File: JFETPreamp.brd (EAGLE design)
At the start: 52.7 x 27.6 mm, 30 parts, among them IC1 ICL7660CBA, IC2 LF356MX, IC3 LF356MX, J1 Input, J2 5V In, J3 Range Select, J4 Output

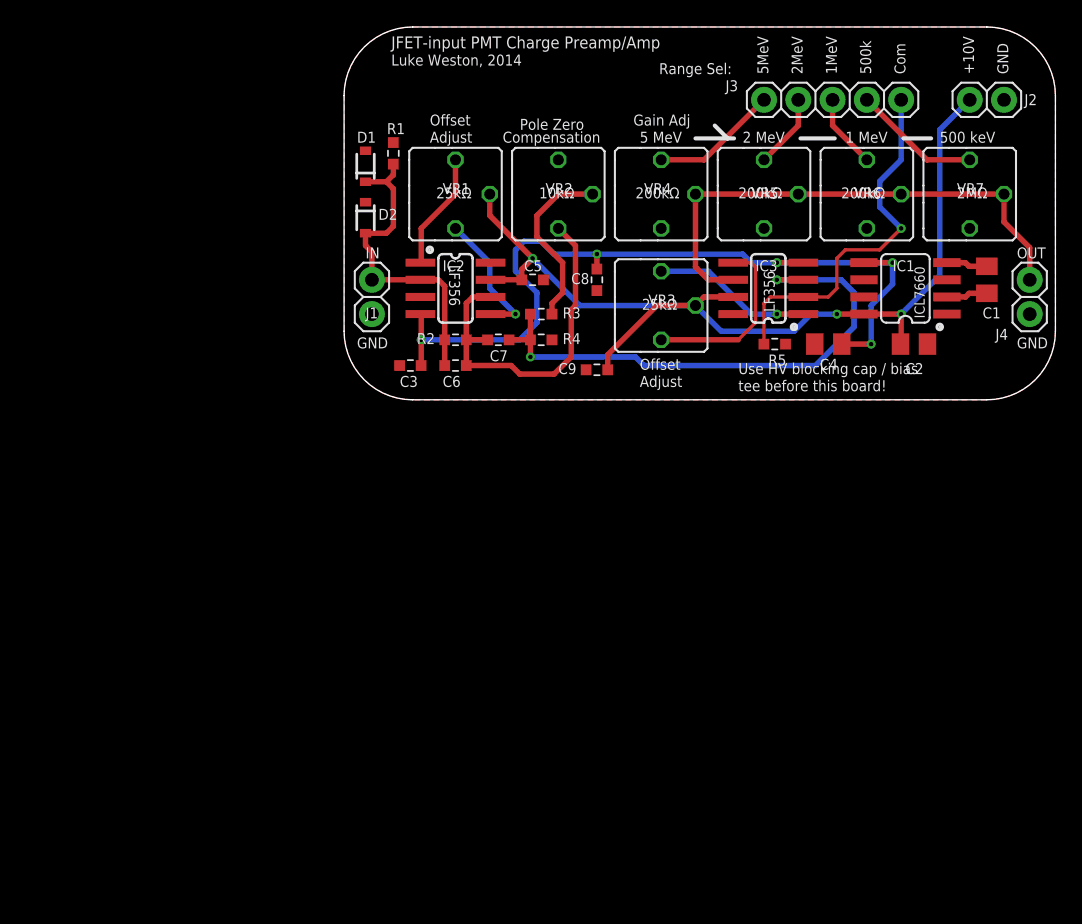
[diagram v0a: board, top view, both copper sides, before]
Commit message: changed to single dual opamp
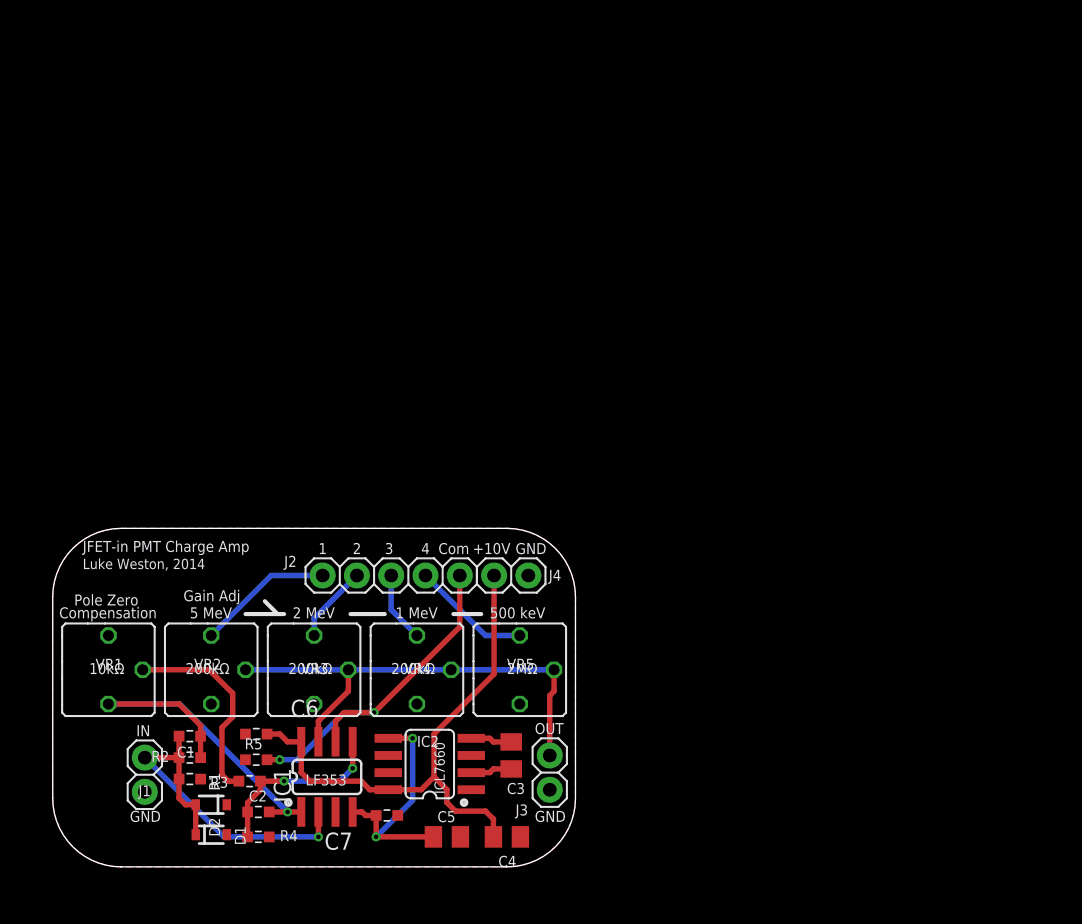
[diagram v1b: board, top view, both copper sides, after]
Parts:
- removed C8, C9: 68nF, freetronics-luke:0603
- removed IC3: LF356MX, linear:SO08
- removed VR6: 200kΩ, pot:B25P
- removed VR7: 2MΩ, pot:B25P
- C1, C2: value 10µF -> 110pF; device rcl:C0805K -> freetronics-luke:0603
- C3, C5: value 68nF -> 10µF; device freetronics-luke:0603 -> rcl:C0805K
- C6, C7: value 110pF -> 68nF
- IC1: value ICL7660CBA -> LF353D; device maxim:SO08 -> linear:SO08
- IC2: value LF356MX -> ICL7660CBA; device linear:SO08 -> maxim:SO08
- J2: value 5V In -> Range Select; device pinhead:1X02 -> pinhead:1X05
- J3: value Range Select -> Output; device pinhead:1X05 -> pinhead:1X02
- J4: value Output -> 5V In
- VR1: value 25kΩ -> 10kΩ
- VR2: value 10kΩ -> 200kΩ
- VR3: value 25kΩ -> 200kΩ
- VR5: value 200kΩ -> 2MΩ
- moved C1 68.1 mm to (12.1, 11.9), turned to 0 degrees
- moved C2 59.7 mm to (17.1, 6.29), turned to 180 degrees
- moved J2 56.5 mm to (27.0, 23.8), turned to 180 degrees
- moved IC1 56.1 mm to (22.2, 8.89), turned to 0 degrees
- moved J3 54.1 mm to (38.7, 9.21), turned to 270 degrees
- moved D1 50.8 mm to (13.7, 4.60), turned to 0 degrees
- moved R5 49.2 mm to (17.0, 10.2), turned to 180 degrees
- moved R1 48.8 mm to (12.1, 8.73), turned to 180 degrees
- moved D2 45.0 mm to (13.7, 6.83), turned to 180 degrees
- moved VR1 43.6 mm to (6.03, 16.8)
- moved VR2 43.6 mm to (13.7, 16.8)
- moved J4 43.6 mm to (35.9, 23.8), turned to 0 degrees
- moved C4 43.6 mm to (35.6, 4.45), turned to 0 degrees
- moved R4 42.4 mm to (17.1, 4.45)
- moved C5 41.8 mm to (31.1, 4.45), turned to 0 degrees
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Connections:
- removed net +5V: C2.1, C5.2, C9.2, IC1.8, IC2.7, IC3.7, J2.1, VR1.S, VR3.S
- removed net -5V: C3.2, C4.1, C8.2, IC1.5, IC2.4, IC3.4
- removed net N$12: IC3.5, VR3.E
- removed net N$14: IC2.5, VR1.E
- net GND: now also C5.2, C6.1, C7.1, J3.2, VR1.A; no longer C2.2, C3.1, C5.1, C8.1, C9.1, J2.2, VR2.A
- net N$1: now also C1.1, IC1.2; no longer C6.1, IC2.2
- net N$10: now also J2.2, VR5.A; no longer J3.2, VR7.A
- net N$11: now also C5.1, C7.2, IC1.4, IC2.5; no longer IC3.1, VR3.A
- net N$13: now also C4.1, C6.2, IC1.8, IC2.8, J4.1; no longer IC2.1, VR1.A
- net N$15: now also C3.1, IC2.2; no longer C1.1, IC1.2
- net N$16: now also C3.2, IC2.4; no longer C1.2, IC1.4
- net N$2: now also C2.2, IC1.5; no longer C7.2, IC3.3
- net N$3: now also C1.2, C2.1, IC1.1, VR1.E; no longer C6.2, C7.1, IC2.6, VR2.E
- net N$4: now also IC1.6, J2.1; no longer IC3.2, J3.1
- net N$5: now also VR1.S; no longer VR2.S
- net N$6: now also J2.5, VR2.A; no longer J3.5, VR4.A
- net N$7: now also IC1.7, J3.1, VR2.S, VR3.S; no longer IC3.6, J4.1, VR6.S, VR7.S
- net N$8: now also J2.4, VR3.A; no longer J3.4, VR5.A
- net N$9: now also J2.3, VR4.A; no longer J3.3, VR6.A
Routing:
- net +5V: track 73.3 -> 0.00 mm, vias 3 -> 0
- net -5V: track 61.9 -> 0.00 mm, vias 5 -> 0
- net N$13: track 8.70 -> 40.1 mm
- net N$2: track 40.8 -> 13.7 mm
- net N$12: track 13.4 -> 0.00 mm
- net N$14: track 10.0 -> 0.00 mm, vias 1 -> 0
- net N$11: track 11.9 -> 17.9 mm, vias 1 -> 2
- net N$1: track 24.0 -> 27.9 mm, vias 0 -> 1
- net N$7: track 39.2 -> 35.6 mm
- net N$5: track 13.2 -> 15.2 mm
- net N$3: track 26.9 -> 28.8 mm, vias 0 -> 1
- net N$4: track 27.6 -> 26.8 mm, vias 1 -> 2
- net N$6: track 9.46 -> 10.1 mm
- net N$10: track 9.46 -> 8.83 mm
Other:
- board size 52.7 x 27.6 mm -> 38.7 x 25.1 mm
- board text added: "1"
- board text added: "2"
- board text added: "3"
- board text added: "4"
- board text added: "JFET-in PMT Charge Amp"
- board text added: "LF353"
- board text removed: "1MeV"
- board text removed: "25kΩ"
- board text removed: "2MeV"
- board text removed: "500k"
- board text removed: "5MeV"
- board text removed: "Adjust"
- board text removed: "JFET-input PMT Charge Preamp/Amp"
- board text removed: "LF356"
- board text removed: "Offset"
- board text removed: "Range Sel:"
- board text removed: "Use HV blocking cap / bias"
- board text removed: "tee before this board!"

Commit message: foo
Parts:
- moved C4 0.95 mm to (34.6, 4.45)
- moved C5 0.95 mm to (30.2, 4.45)
- moved J3 0.32 mm to (39.1, 9.21)
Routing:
- net N$4: track 26.8 -> 31.0 mm
- net N$1: track 27.9 -> 24.4 mm, vias 1 -> 0
- net N$11: track 17.9 -> 17.0 mm
- net N$13: track 40.1 -> 39.3 mm

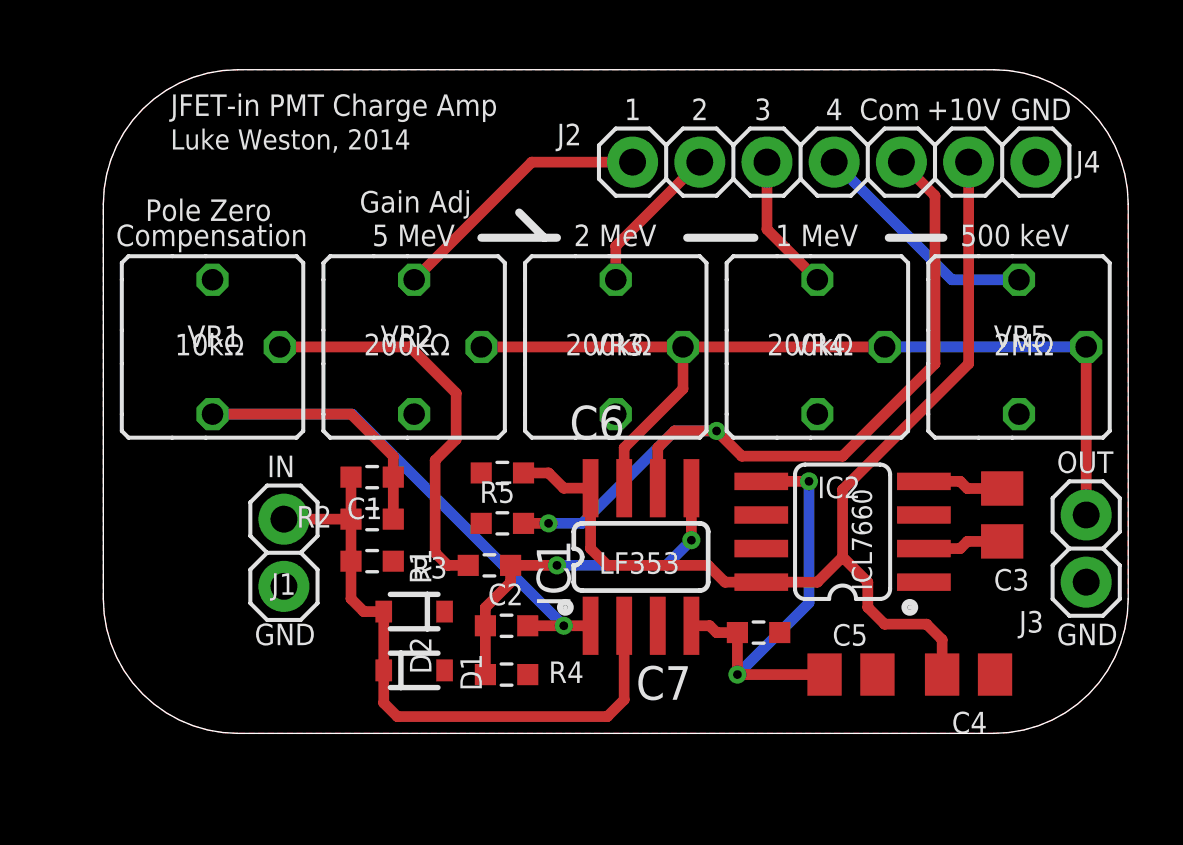
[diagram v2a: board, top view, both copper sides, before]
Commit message: changed selector switch footprint
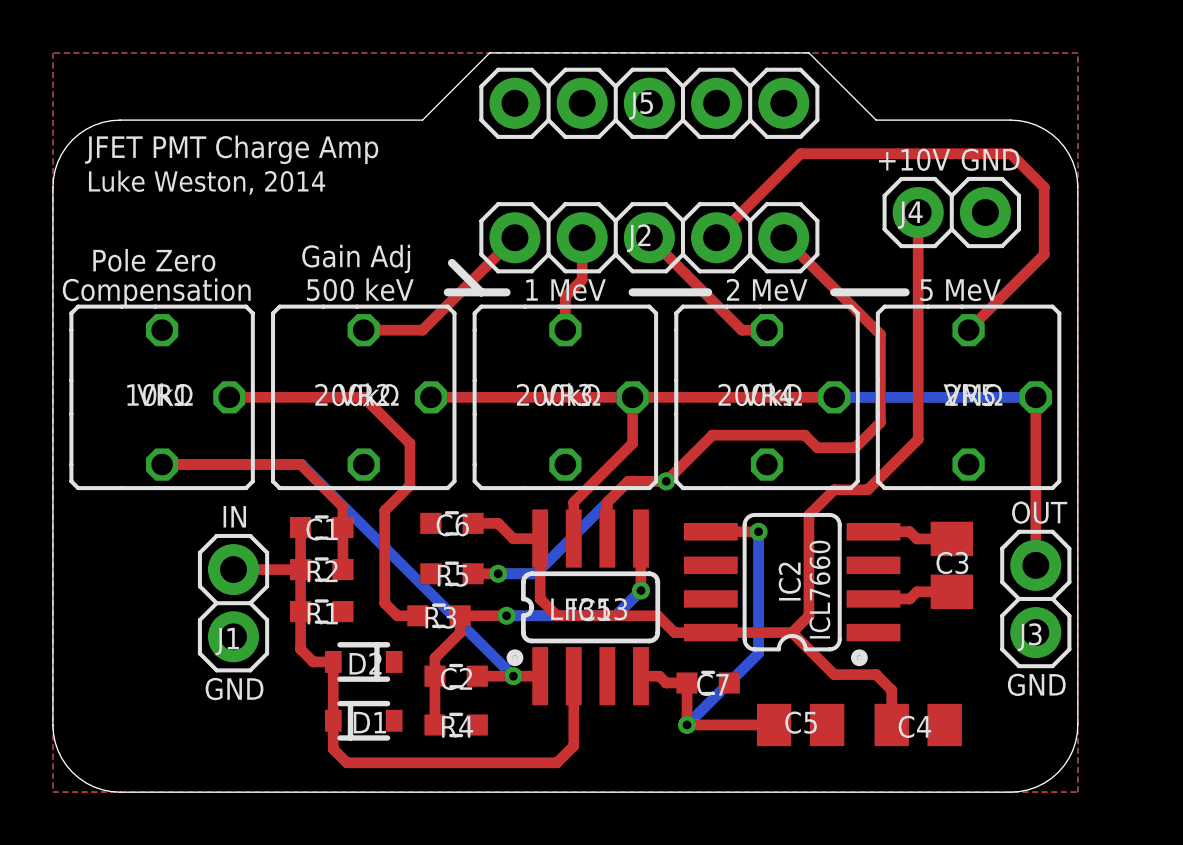
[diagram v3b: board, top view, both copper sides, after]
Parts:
- added J5: Range Select, pinhead:1X05
- J4: value 5V In -> Pwr In
- moved J2 5.28 mm to (22.5, 21.0)
- moved J4 2.69 mm to (34.0, 21.9)
- moved VR3 2.69 mm to (19.4, 14.9)
- moved VR5 2.69 mm to (34.6, 14.9)
- moved C3 2.69 mm to (34.0, 8.57)
- moved C4 2.69 mm to (32.7, 2.54)
- moved C5 2.69 mm to (28.3, 2.54)
- moved C7 2.69 mm to (24.8, 4.13)
- moved IC1 2.69 mm to (20.3, 6.99)
- moved J3 2.69 mm to (37.1, 7.30)
- moved VR1 2.69 mm to (4.13, 14.9)
- moved VR2 2.69 mm to (11.7, 14.9)
- moved C2 2.69 mm to (15.2, 4.38)
- moved D2 2.69 mm to (11.7, 4.92)
- moved J1 2.69 mm to (6.83, 7.14)
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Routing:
- net N$10: track 8.83 -> 20.8 mm
- net N$6: track 10.1 -> 7.16 mm
- net N$8: track 5.76 -> 3.76 mm
- net N$9: track 5.23 -> 5.89 mm
- added copper zone on layer 16, net GND
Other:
- board size 38.7 x 25.1 mm -> 38.7 x 27.9 mm
- board text added: "JFET PMT Charge Amp"
- board text removed: "1"
- board text removed: "2"
- board text removed: "3"
- board text removed: "4"
- board text removed: "Com"
- board text removed: "JFET-in PMT Charge Amp"
